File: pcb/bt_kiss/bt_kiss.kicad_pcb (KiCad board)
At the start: 2 copper layers, 30 x 150 mm, 18 parts, among them J1 HC-05, J2 to_radio, J3 5v PWR, J4 Bat_Plus, J5 Bat_GND, J6 Bat input, J7 Key, Q1 PN2222A, SW1 SW_Push

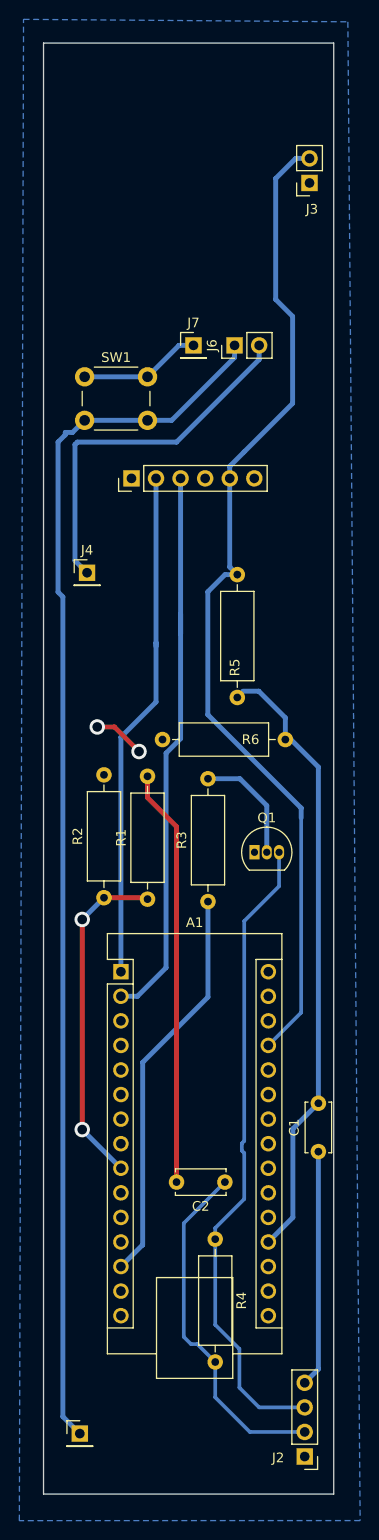
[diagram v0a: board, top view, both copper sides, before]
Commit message: added 18650 battery holder for the BT KISS TNC PCB
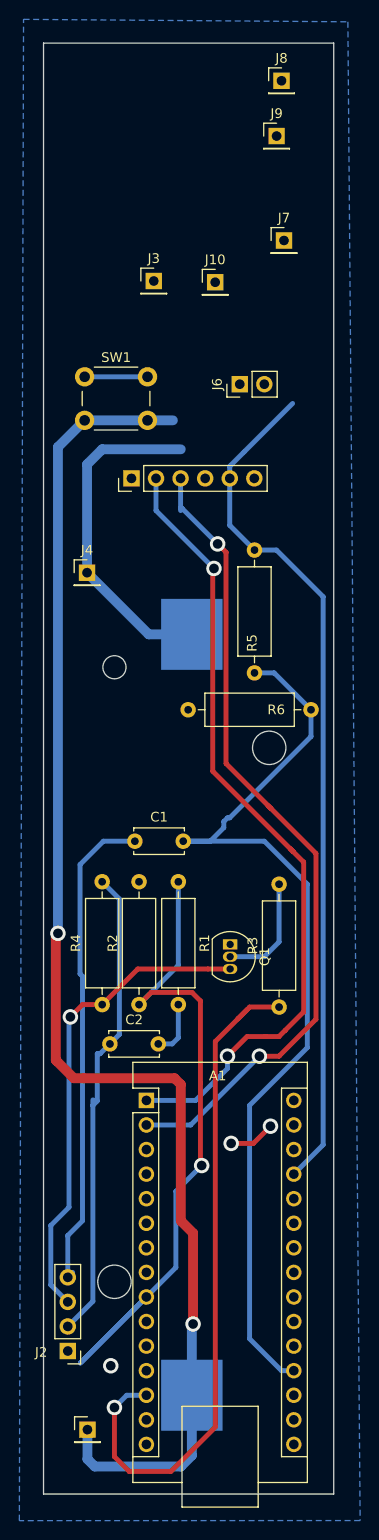
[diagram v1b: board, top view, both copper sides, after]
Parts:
- added BT1: Battery_Cell, Battery:BatteryHolder_Keystone_1042_1x18650, B.Cu at (60.8, 121.7)
- added J10: Bat_Plus, Connector_PinHeader_2.54mm:PinHeader_1x01_P2.54mm_Vertical, F.Cu at (63.2, 46.0)
- added J8: 5V, Connector_PinHeader_2.54mm:PinHeader_1x01_P2.54mm_Vertical, F.Cu at (70.1, 25.1)
- added J9: GND, Connector_PinHeader_2.54mm:PinHeader_1x01_P2.54mm_Vertical, F.Cu at (69.6, 30.9)
- J3: value 5v PWR -> Bat_GND; footprint Connector_PinSocket_2.54mm:PinSocket_1x02_P2.54mm_Vertical -> Connector_PinHeader_2.54mm:PinHeader_1x01_P2.54mm_Vertical
- moved C1 37.3 mm to (54.9, 103.8), turned to 0 degrees
- moved R4 26.9 mm to (51.6, 120.7), turned to 90 degrees
- moved J2 26.8 mm to (48.0, 156.5)
- moved J3 19.0 mm to (56.9, 45.8), turned to 0 degrees
- moved C2 18.6 mm to (52.4, 124.7), turned to 0 degrees
- moved J7 14.3 mm to (70.4, 41.7)
- moved A1 13.6 mm to (56.1, 130.6)
- moved R3 13.1 mm to (69.8, 120.9)
- moved R2 11.6 mm to (55.4, 120.7)
- moved Q1 9.85 mm to (64.8, 114.4), turned to -90 degrees
- moved R6 4.06 mm to (73.2, 90.2)
- moved J6 4.05 mm to (65.8, 56.5)
- moved R1 3.66 mm to (59.4, 108.0), turned to -90 degrees
- moved R5 3.10 mm to (67.3, 73.7)
- moved J5 0.89 mm to (50.0, 164.6)
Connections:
- J3 pad 1: GND -> Net-(BT1--)
- J5 pad 1: Net-(J5-Pin_1) -> Net-(BT1--)
- J6 pad 1: Net-(J5-Pin_1) -> Net-(BT1--)
- SW1 pad 2: Net-(J5-Pin_1) -> Net-(BT1--)
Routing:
- net Net-(BT1--): track 0.00 -> 144.0 mm, vias 0 -> 2
- net Net-(J5-Pin_1): track 126.7 -> 0.00 mm
- net Net-(A1-D6): track 35.1 -> 73.9 mm, vias 2 -> 1
- net Net-(C2-Pad2): track 43.2 -> 5.76 mm
- net Net-(A1-A0): track 63.6 -> 98.3 mm
- net Net-(A1-D10): track 41.5 -> 71.5 mm, vias 0 -> 1
- net Net-(A1-D1/TX): track 52.9 -> 82.8 mm, vias 0 -> 2
- net audio_out: track 24.5 -> 50.8 mm
- net Net-(A1-D0/RX): track 59.2 -> 84.5 mm, vias 0 -> 2
- net PTT: track 66.9 -> 49.3 mm, vias 0 -> 1
- net VCC: track 105.1 -> 89.0 mm
- net audio_in: track 36.5 -> 49.7 mm
- net Net-(J7-Pin_1): track 12.6 -> 6.50 mm
- net Net-(BT1-+): track 37.9 -> 35.0 mm
- net GND: track 5.37 -> 4.80 mm, vias 2 -> 3

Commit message: added KISS TNC read me: 2025-04-07 18:54:28
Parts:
- removed J6: Bat input, Connector_PinHeader_2.54mm:PinHeader_1x02_P2.54mm_Vertical
- J1: moved to B.Cu
- moved J1 13.4 mm to (68.0, 66.2)
- moved J8 6.22 mm to (68.0, 31.0)
- moved J9 6.07 mm to (68.0, 25.0)
- moved J7 2.14 mm to (69.0, 40.0)
- moved J10 1.97 mm to (63.2, 44.0)
- moved J3 1.85 mm to (57.0, 44.0)
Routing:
- net VCC: track 89.0 -> 132.5 mm, vias 0 -> 2
- net Net-(J7-Pin_1): track 6.50 -> 37.8 mm
- net Net-(BT1-+): track 35.0 -> 62.2 mm
- net Net-(BT1--): track 144.0 -> 164.7 mm
- net Net-(A1-D0/RX): track 84.5 -> 87.0 mm, vias 2 -> 3
- net Net-(A1-D1/TX): track 82.8 -> 81.3 mm, vias 2 -> 1

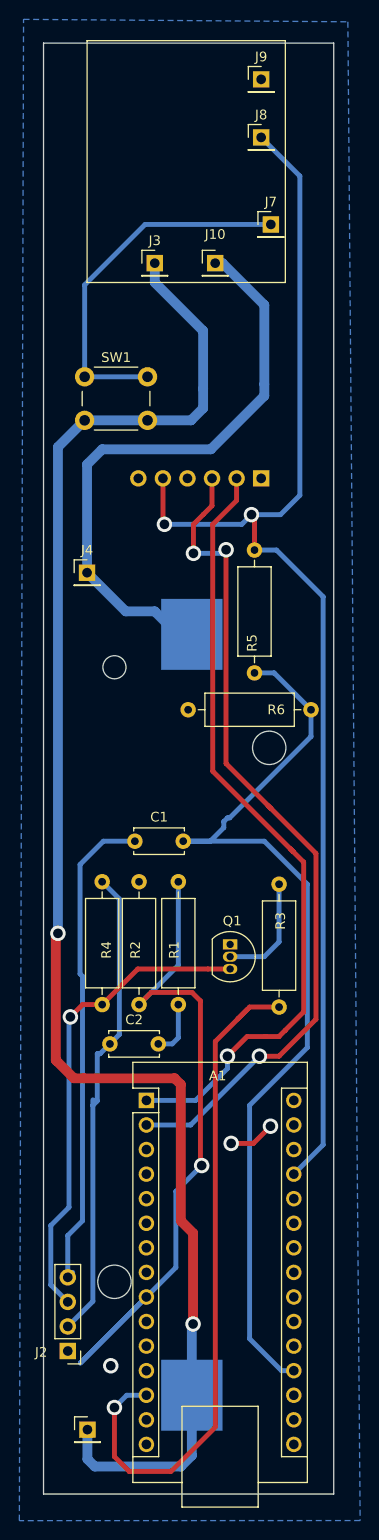
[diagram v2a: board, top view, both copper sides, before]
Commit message: BT TNC v1.1 added ready for production
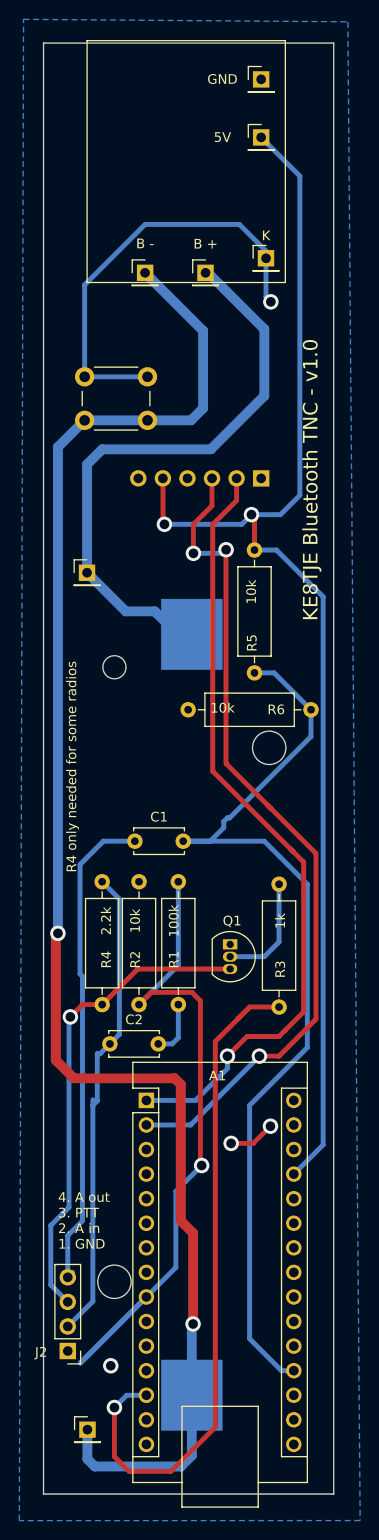
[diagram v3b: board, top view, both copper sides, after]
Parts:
- B +: renamed from J10
- B -: renamed from J3
- moved K 3.54 mm to (68.5, 43.5)
- moved B - 1.41 mm to (56.0, 45.0)
- moved B + 1.41 mm to (62.2, 45.0)
- renumbered J8 to 5V, J9 to GND, J7 to K
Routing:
- net Net-(J7-Pin_1): track 37.8 -> 44.6 mm, vias 0 -> 1
- net Net-(BT1-+): track 62.2 -> 61.3 mm
- net Net-(BT1--): track 164.7 -> 164.2 mm
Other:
- board text added: "4. A out 3. PTT 2. A in 1. GND"
- board text added: "KE8TJE Bluetooth TNC - v1.0"
- board text added: "R4 only needed for some radios"
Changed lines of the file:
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@@
 		(legacy_teardrops no)
 	)
-	(paper "A4")
+	(paper "USLetter")
 	(layers
 		(0 "F.Cu" signal)
@@
 		(pad_to_mask_clearance 0)
 		(allow_soldermask_bridges_in_footprints no)
+		(grid_origin 56.75 44.25)
 		(pcbplotparams
 			(layerselection 0x00010fc_ffffffff)
@@
 		)
 		(property "Value" "10k"
-			(at 5.85 3 0)
-			(layer "F.Fab")
+			(at 9.152 0.17 0)
+			(layer "F.SilkS")
 			(effects
 				(font
@@
 		(tags "Resistor Axial_DIN0309 series Axial Horizontal pin pitch 12.7mm 0.5W = 1/2W length 9mm diameter 3.2mm")
 		(property "Reference" "R3"
-			(at 8.904 0.15 90)
+			(at 3.904 0.15 90)
 			(layer "F.SilkS")
 			(effects
@@
 		)
 		(property "Value" "1k"
-			(at -1.5 -4.5 90)
-			(layer "F.Fab")
+			(at 8.904 0.15 90)
+			(layer "F.SilkS")
 			(effects
 				(font
@@
 		(descr "Through hole straight pin header, 1x01, 2.54mm pitch, single row")
 		(tags "Through hole pin header THT 1x01 2.54mm single row")
-		(property "Reference" "J9"
-			(at 0 -2.33 0)
+		(property "Reference" "GND"
+			(at -4 0 0)
 			(layer "F.SilkS")
 			(effects
@@
 	(footprint "Connector_PinHeader_2.54mm:PinHeader_1x01_P2.54mm_Vertical"
 		(layer "F.Cu")
-		(at 63.246 44)
+		(at 62.25 45)
 		(descr "Through hole straight pin header, 1x01, 2.54mm pitch, single row")
 		(tags "Through hole pin header THT 1x01 2.54mm single row")
-		(property "Reference" "J10"
+		(property "Reference" "B +"
 			(at 0 -2.974 0)
 			(layer "F.SilkS")
@@
 	(footprint "Connector_PinHeader_2.54mm:PinHeader_1x01_P2.54mm_Vertical"
 		(layer "F.Cu")
-		(at 57 44)
+		(at 56 45)
 		(descr "Through hole straight pin header, 1x01, 2.54mm pitch, single row")
 		(tags "Through hole pin header THT 1x01 2.54mm single row")
-		(property "Reference" "J3"
-			(at 0 -2.33 0)
+		(property "Reference" "B -"
+			(at 0 -3 0)
 			(layer "F.SilkS")
 			(effects
@@
 	(footprint "Connector_PinHeader_2.54mm:PinHeader_1x01_P2.54mm_Vertical"
 		(layer "F.Cu")
-		(at 69 40)
+		(at 68.5 43.5)
 		(descr "Through hole straight pin header, 1x01, 2.54mm pitch, single row")
 		(tags "Through hole pin header THT 1x01 2.54mm single row")
-		(property "Reference" "J7"
+		(property "Reference" "K"
 			(at 0 -2.33 0)
 			(layer "F.SilkS")
@@
 		)
 		(property "Value" "Key"
-			(at 0 2.33 0)
+			(at -0.25 2.33 0)
 			(layer "F.Fab")
 			(effects
@@
 		(tags "Resistor Axial_DIN0309 series Axial Horizontal pin pitch 12.7mm 0.5W = 1/2W length 9mm diameter 3.2mm")
 		(property "Reference" "R2"
-			(at 5.65 -0.372 90)
+			(at 4.65 -0.372 90)
 			(layer "F.SilkS")
 			(effects
@@
 		(property "Value" "10k"
 			(at 8.65 -0.372 90)
-			(layer "F.Fab")
+			(layer "F.SilkS")
 			(effects
 				(font
@@
 		(property "Value" "10k"
 			(at 4.34 0.31 90)
-			(layer "F.Fab")
+			(layer "F.SilkS")
 			(effects
 				(font
@@
 		(tags "Resistor Axial_DIN0309 series Axial Horizontal pin pitch 12.7mm 0.5W = 1/2W length 9mm diameter 3.2mm")
 		(property "Reference" "R4"
-			(at 5.65 0.438 90)
+			(at 4.65 0.438 90)
 			(layer "F.SilkS")
 			(effects
@@
 		(property "Value" "2.2k"
 			(at 8.65 0.438 90)
-			(layer "F.Fab")
+			(layer "F.SilkS")
 			(effects
 				(font
@@
 		(tags "Resistor Axial_DIN0309 series Axial Horizontal pin pitch 12.7mm 0.5W = 1/2W length 9mm diameter 3.2mm")
 		(property "Reference" "R1"
-			(at 7.05 0.436 90)
+			(at 8.05 0.436 90)
 			(layer "F.SilkS")
 			(effects
@@
 		(property "Value" "100k"
 			(at 4.05 0.436 90)
-			(layer "F.Fab")
+			(layer "F.SilkS")
 			(effects
 				(font
@@
 			(at 0 -2.33 0)
 			(layer "F.SilkS")
+			(hide yes)
 			(effects
 				(font
@@
 			(at 3.25 -2 0)
 			(layer "F.SilkS")
+			(hide yes)
 			(effects
 				(font
@@
 		(descr "Through hole straight pin header, 1x01, 2.54mm pitch, single row")
 		(tags "Through hole pin header THT 1x01 2.54mm single row")
-		(property "Reference" "J8"
-			(at 0 -2.33 0)
+		(property "Reference" "5V"
+			(at -4 0 0)
 			(layer "F.SilkS")
 			(effects
@@
 		(layer "Edge.Cuts")
 	)
+	(gr_text "4. A out\n3. PTT\n2. A in\n1. GND"
+		(at 47 146 0)
+		(layer "F.SilkS")
+		(effects
+			(font
+				(size 1 1)
+				(thickness 0.15)
+			)
+			(justify left bottom)
+		)
+	)
+	(gr_text "R4 only needed for some radios"
+		(at 49 107 90)
+		(layer "F.SilkS")
+		(effects
+			(font
+				(size 1 1)
+				(thickness 0.15)
+			)
+			(justify left bottom)
+		)
+	)
+	(gr_text "KE8TJE Bluetooth TNC - v1.0"
+		(at 74 81 90)
+		(layer "F.SilkS")
+		(effects
+			(font
+				(size 1.5 1.5)
+				(thickness 0.15)
+			)
+			(justify left bottom)
+		)
+	)
 	(segment
 		(start 68.326 103.759)
@@
 		(net 35)
 	)
+	(via
+		(at 69 48)
+		(size 1.6)
+		(drill 1)
+		(layers "F.Cu" "B.Cu")
+		(net 36)
+	)
+	(segment
+		(start 65.75 40)
+		(end 68.5 42.75)
+		(width 0.508)
+		(layer "B.Cu")
+		(net 36)
+	)
+	(segment
+		(start 68.5 42.75)
+		(end 68.5 47.5)
+		(width 0.508)
+		(layer "B.Cu")
+		(net 36)
+	)
 	(segment
 		(start 49.75 55.75)
@@
 	)
 	(segment
-		(start 56 40)
+		(start 49.75 55.75)
 		(end 49.75 46.25)
 		(width 0.508)
@@
 	)
 	(segment
-		(start 69 40)
-		(end 56 40)
+		(start 68.5 43.5)
+		(end 69 44)
+		(width 0.508)
+		(layer "B.Cu")
+		(net 36)
+	)
+	(segment
+		(start 68.5 47.5)
+		(end 69 48)
+		(width 0.508)
+		(layer "B.Cu")
+		(net 36)
+	)
+	(segment
+		(start 56 40)
+		(end 65.75 40)
 		(width 0.508)
 		(layer "B.Cu")
@@
 	(segment
 		(start 49.75 46.25)
-		(end 49.75 55.75)
+		(end 56 40)
 		(width 0.508)
 		(layer "B.Cu")
@@
 	)
 	(segment
-		(start 57 46)
-		(end 62 51)
+		(start 50.038 167.64)
+		(end 50.038 164.592)
 		(width 1.016)
 		(layer "B.Cu")
@@
 	(segment
 		(start 62 59)
-		(end 62 57)
-		(width 1.016)
-		(layer "B.Cu")
-		(net 38)
-	)
-	(segment
-		(start 50.038 167.64)
-		(end 50.038 164.592)
+		(end 60.75 60.25)
 		(width 1.016)
 		(layer "B.Cu")
@@
 	)
 	(segment
-		(start 60.75 60.25)
-		(end 62 59)
-		(width 1.016)
-		(layer "B.Cu")
-		(net 38)
-	)
-	(segment
 		(start 60.832 167.26)
 		(end 59.69 168.402)
@@
 	)
 	(segment
-		(start 60.832 161.036)
-		(end 60.832 153.798)
+		(start 62 51)
+		(end 62 59)
 		(width 1.016)
 		(layer "B.Cu")
@@
 	)
 	(segment
-		(start 59.69 168.402)
-		(end 50.8 168.402)
+		(start 60.832 161.036)
+		(end 60.832 153.798)
 		(width 1.016)
 		(layer "B.Cu")
@@
 	)
 	(segment
-		(start 60.832 161.036)
-		(end 60.832 167.26)
+		(start 56 45)
+		(end 62 51)
 		(width 1.016)
 		(layer "B.Cu")
@@
 	)
 	(segment
-		(start 46.99 63.01)
-		(end 49.75 60.25)
+		(start 59.69 168.402)
+		(end 50.8 168.402)
 		(width 1.016)
 		(layer "B.Cu")
@@
 	)
 	(segment
-		(start 62 57)
-		(end 62 51)
+		(start 60.832 161.036)
+		(end 60.832 167.26)
 		(width 1.016)
 		(layer "B.Cu")
@@
 	)
 	(segment
-		(start 57 44)
-		(end 57 46)
+		(start 46.99 63.01)
+		(end 49.75 60.25)
 		(width 1.016)
 		(layer "B.Cu")
@@
 	)
 	(segment
-		(start 56.25 60.25)
-		(end 60.75 60.25)
+		(start 60.75 60.25)
+		(end 56.25 60.25)
 		(width 1.016)
 		(layer "B.Cu")
@@
 	)
 	(segment
-		(start 60.832 82.376)
-		(end 59.376 82.376)
+		(start 50 76)
+		(end 50 64.808)
 		(width 1.016)
 		(layer "B.Cu")
@@
 	)
 	(segment
-		(start 50 76)
-		(end 50 64.808)
+		(start 60.832 82.376)
+		(end 59.376 82.376)
 		(width 1.016)
 		(layer "B.Cu")
@@
 	)
 	(segment
-		(start 59.376 82.376)
-		(end 57 80)
+		(start 68.326 57.717081)
+		(end 68.326 50.826)
 		(width 1.016)
 		(layer "B.Cu")
@@
 	)
 	(segment
-		(start 68.326 48.326)
-		(end 64 44)
-		(width 1.016)
-		(layer "B.Cu")
-		(net 39)
-	)
-	(segment
-		(start 68.326 57.717081)
-		(end 68.326 56.515)
+		(start 68.326 50.826)
+		(end 62.5 45)
 		(width 1.016)
 		(layer "B.Cu")
@@
 	)
 	(segment
-		(start 50 64.808)
-		(end 51.562 63.246)
+		(start 59.376 82.376)
+		(end 57 80)
 		(width 1.016)
 		(layer "B.Cu")
@@
 	)
 	(segment
-		(start 68.326 56.515)
-		(end 68.326 48.326)
+		(start 62.5 45)
+		(end 62.25 45)
 		(width 1.016)
 		(layer "B.Cu")
@@
 	)
 	(segment
-		(start 64 44)
-		(end 63.246 44)
+		(start 50 64.808)
+		(end 51.562 63.246)
 		(width 1.016)
 		(layer "B.Cu")
